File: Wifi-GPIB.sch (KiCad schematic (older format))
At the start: 10 parts

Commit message: Add ESP to sch
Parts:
- added U?: ESP-12/07v2/08v2, symbol ESP-12/07v2/08v2
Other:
- moved on the sheet: P?, U?
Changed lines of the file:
@@
 LIBS:open-project
 LIBS:mic5504
+LIBS:esp8266
+LIBS:Wifi-GPIB-cache
 EELAYER 25 0
 EELAYER END
@@
 L STM32F030C6 U?
 U 1 1 5564BC8B
-P 3950 4100
-F 0 "U?" H 2450 6000 60  0000 C CNN
-F 1 "STM32F030C6" H 5200 2200 60  0000 C CNN
-F 2 "LQFP48" H 3950 4100 40  0000 C CIN
-F 3 "" H 3950 4100 60  0000 C CNN
-	1    3950 4100
+P 2900 4550
+F 0 "U?" H 1400 6450 60  0000 C CNN
+F 1 "STM32F030C6" H 4150 2650 60  0000 C CNN
+F 2 "LQFP48" H 2900 4550 40  0000 C CIN
+F 3 "" H 2900 4550 60  0000 C CNN
+	1    2900 4550
 	1    0    0    -1
 $EndComp
@@
 L SN75160B U?
 U 1 1 5564BDA6
-P 7950 2350
-F 0 "U?" H 7950 2250 50  0000 C CNN
-F 1 "SN75160B" H 7950 2450 50  0000 C CNN
-F 2 "MODULE" H 7950 2350 50  0001 C CNN
-F 3 "DOCUMENTATION" H 7950 2350 50  0001 C CNN
-	1    7950 2350
+P 6950 3550
+F 0 "U?" H 6950 3450 50  0000 C CNN
+F 1 "SN75160B" H 6950 3650 50  0000 C CNN
+F 2 "MODULE" H 6950 3550 50  0001 C CNN
+F 3 "DOCUMENTATION" H 6950 3550 50  0001 C CNN
+	1    6950 3550
 	1    0    0    -1
 $EndComp
@@
 L SN75162B U?
 U 1 1 5564BE4F
-P 7950 4300
-F 0 "U?" H 7950 4200 50  0000 C CNN
-F 1 "SN75162B" H 7950 4400 50  0000 C CNN
-F 2 "MODULE" H 7950 4300 50  0001 C CNN
-F 3 "DOCUMENTATION" H 7950 4300 50  0001 C CNN
-	1    7950 4300
+P 6950 5500
+F 0 "U?" H 6950 5400 50  0000 C CNN
+F 1 "SN75162B" H 6950 5600 50  0000 C CNN
+F 2 "MODULE" H 6950 5500 50  0001 C CNN
+F 3 "DOCUMENTATION" H 6950 5500 50  0001 C CNN
+	1    6950 5500
 	1    0    0    -1
 $EndComp
@@
 L CONN_CENTRONICS_24 P?
 U 1 1 5564D4E2
-P 10350 3300
-F 0 "P?" H 10350 3950 60  0000 C CNN
-F 1 "CONN_CENTRONICS_24" V 10350 3300 50  0000 C CNN
-F 2 "" H 10350 3300 60  0000 C CNN
-F 3 "" H 10350 3300 60  0000 C CNN
-	1    10350 3300
+P 10300 3750
+F 0 "P?" H 10300 4400 60  0000 C CNN
+F 1 "CONN_CENTRONICS_24" V 10300 3750 50  0000 C CNN
+F 2 "" H 10300 3750 60  0000 C CNN
+F 3 "" H 10300 3750 60  0000 C CNN
+	1    10300 3750
 	1    0    0    -1
 $EndComp
@@
 	1    0    0    -1
 $EndComp
+$Comp
+L ESP-12/07v2/08v2 U?
+U 1 1 5564D82B
+P 5450 1600
+F 0 "U?" H 5450 2150 60  0000 C CNN
+F 1 "ESP-12/07v2/08v2" H 5450 1050 60  0000 C CNN
+F 2 "" H 5450 1600 60  0000 C CNN
+F 3 "" H 5450 1600 60  0000 C CNN
+	1    5450 1600
+	1    0    0    -1
+$EndComp

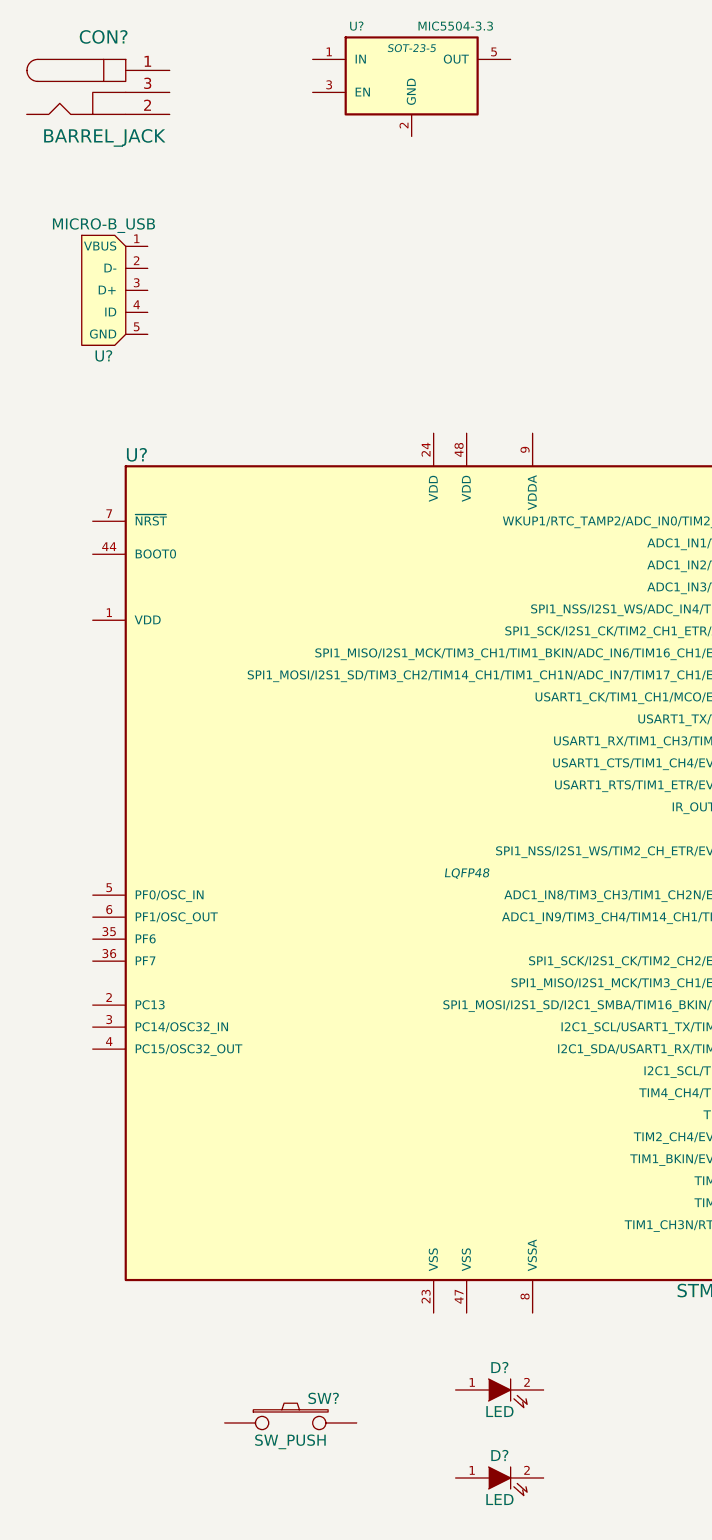
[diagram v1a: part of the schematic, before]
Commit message: Add new voltage regulator to sch
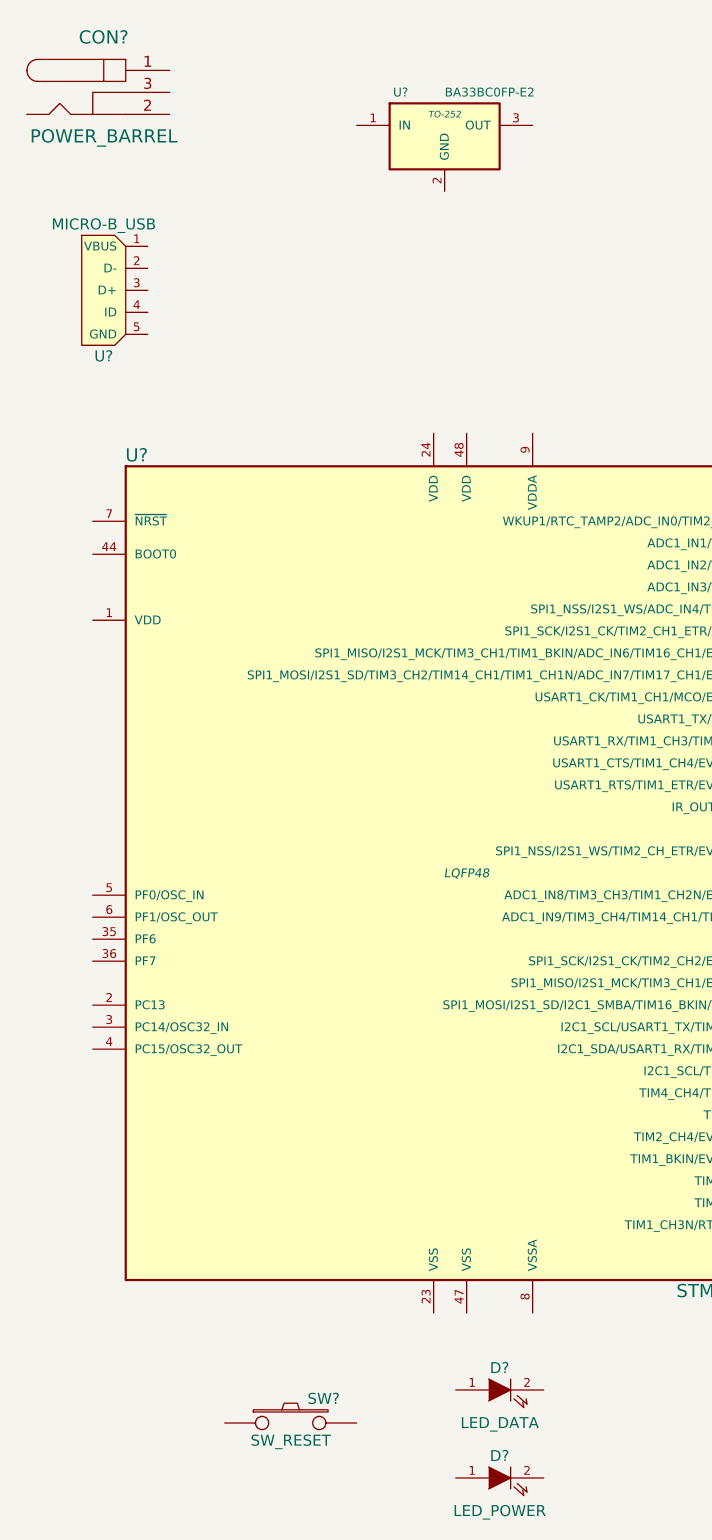
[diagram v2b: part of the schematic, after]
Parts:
- removed U?: MIC5504-3.3, SOT-23-5, symbol MIC5504-3.3
- added U?: BA33BC0FP-E2, TO-252, symbol BA33BC0FP-E2
- CON?: value BARREL_JACK -> POWER_BARREL
- D?: value LED -> LED_DATA
- D?: value LED -> LED_POWER
- SW?: value SW_PUSH -> SW_RESET
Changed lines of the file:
@@
 LIBS:conn_centronics_24
 LIBS:open-project
-LIBS:mic5504
 LIBS:esp8266
+LIBS:ba33bc0fp-e2
 LIBS:Wifi-GPIB-cache
 EELAYER 25 0
@@
 P 2100 7050
 F 0 "SW?" H 2250 7160 50  0000 C CNN
-F 1 "SW_PUSH" H 2100 6970 50  0000 C CNN
+F 1 "SW_RESET" H 2100 6970 50  0000 C CNN
 F 2 "" H 2100 7050 60  0000 C CNN
 F 3 "" H 2100 7050 60  0000 C CNN
@@
 P 3050 6900
 F 0 "D?" H 3050 7000 50  0000 C CNN
-F 1 "LED" H 3050 6800 50  0000 C CNN
+F 1 "LED_DATA" H 3050 6750 50  0000 C CNN
 F 2 "" H 3050 6900 60  0000 C CNN
 F 3 "" H 3050 6900 60  0000 C CNN
@@
 P 3050 7300
 F 0 "D?" H 3050 7400 50  0000 C CNN
-F 1 "LED" H 3050 7200 50  0000 C CNN
+F 1 "LED_POWER" H 3050 7150 50  0000 C CNN
 F 2 "" H 3050 7300 60  0000 C CNN
 F 3 "" H 3050 7300 60  0000 C CNN
@@
 P 1250 1000
 F 0 "CON?" H 1250 1250 60  0000 C CNN
-F 1 "BARREL_JACK" H 1250 800 60  0000 C CNN
+F 1 "POWER_BARREL" H 1250 800 60  0000 C CNN
 F 2 "" H 1250 1000 60  0000 C CNN
 F 3 "" H 1250 1000 60  0000 C CNN
@@
 $EndComp
 $Comp
-L MIC5504-3.3 U?
-U 1 1 5564E907
-P 2650 900
-F 0 "U?" H 2400 1100 40  0000 C CNN
-F 1 "MIC5504-3.3" H 2850 1100 40  0000 C CNN
-F 2 "SOT-23-5" H 2650 1000 35  0000 C CIN
-F 3 "" H 2650 900 60  0000 C CNN
-	1    2650 900
-	1    0    0    -1
-$EndComp
-$Comp
 L ESP-12/07v2/08v2 U?
 U 1 1 5564D82B
@@
 	1    0    0    -1
 $EndComp
+$Comp
+L BA33BC0FP-E2 U?
+U 1 1 5564E643
+P 2800 1200
+F 0 "U?" H 2600 1400 40  0000 C CNN
+F 1 "BA33BC0FP-E2" H 2800 1400 40  0000 L CNN
+F 2 "TO-252" H 2800 1300 30  0000 C CIN
+F 3 "" H 2800 1200 60  0000 C CNN
+	1    2800 1200
+	1    0    0    -1
+$EndComp

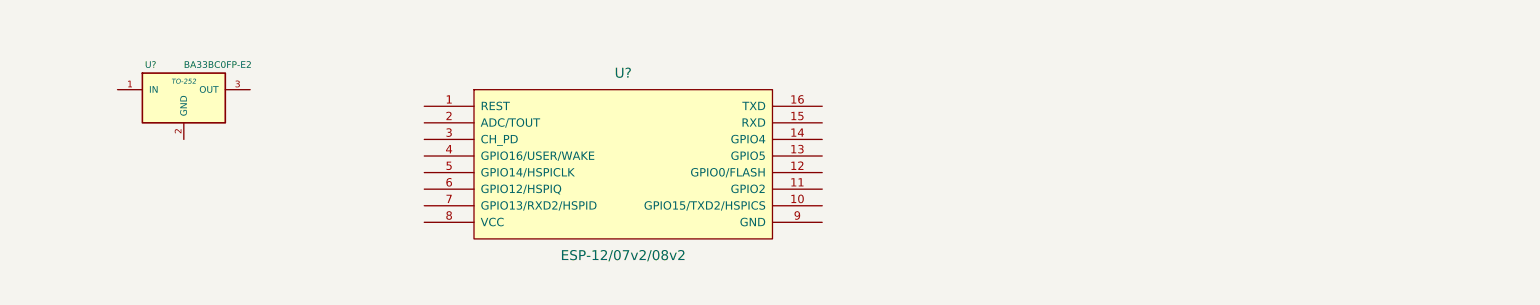
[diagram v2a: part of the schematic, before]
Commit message: Add power test points and add ESP programming header
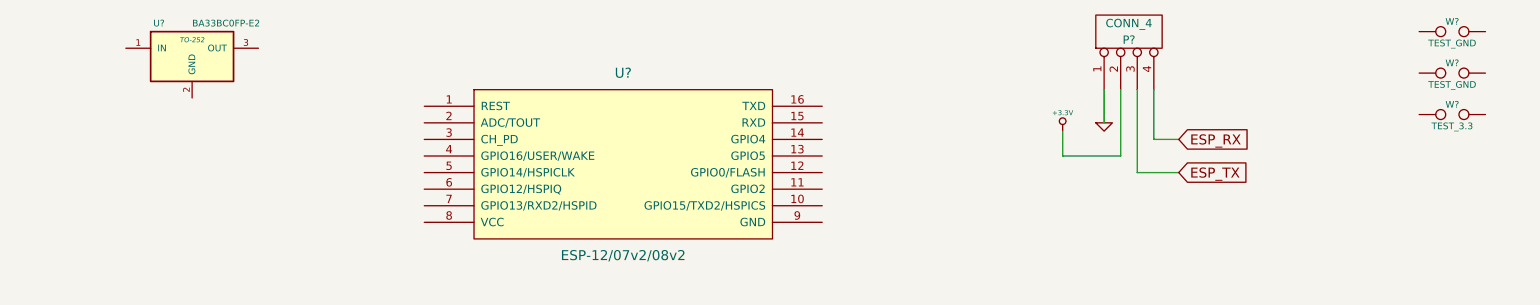
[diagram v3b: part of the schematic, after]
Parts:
- added P?: CONN_4, symbol CONN_4
- added W? (x2): TEST_GND, symbol TEST
- added W?: TEST_3.3, symbol TEST
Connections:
- new net +3.3V: P?.2 (P2)
- new net ESP_RX: P?.4 (P4)
- new net ESP_TX: P?.3 (P3)
- new net GND: P?.1 (P1)
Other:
- moved on the sheet: U?
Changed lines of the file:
@@
 L BA33BC0FP-E2 U?
 U 1 1 5564E643
-P 2800 1200
-F 0 "U?" H 2600 1400 40  0000 C CNN
-F 1 "BA33BC0FP-E2" H 2800 1400 40  0000 L CNN
-F 2 "TO-252" H 2800 1300 30  0000 C CIN
-F 3 "" H 2800 1200 60  0000 C CNN
-	1    2800 1200
+P 2850 950
+F 0 "U?" H 2650 1150 40  0000 C CNN
+F 1 "BA33BC0FP-E2" H 2850 1150 40  0000 L CNN
+F 2 "TO-252" H 2850 1050 30  0000 C CIN
+F 3 "" H 2850 950 60  0000 C CNN
+	1    2850 950
 	1    0    0    -1
 $EndComp
+$Comp
+L CONN_4 P?
+U 1 1 5564EAE9
+P 8500 800
+F 0 "P?" V 8450 800 50  0000 C CNN
+F 1 "CONN_4" V 8550 800 50  0000 C CNN
+F 2 "" H 8500 800 60  0000 C CNN
+F 3 "" H 8500 800 60  0000 C CNN
+	1    8500 800
+	0    -1   -1   0
+$EndComp
+$Comp
+L GND #PWR?
+U 1 1 5564ECD5
+P 8350 1350
+F 0 "#PWR?" H 8350 1350 30  0001 C CNN
+F 1 "GND" H 8350 1280 30  0001 C CNN
+F 2 "" H 8350 1350 60  0000 C CNN
+F 3 "" H 8350 1350 60  0000 C CNN
+	1    8350 1350
+	1    0    0    -1
+$EndComp
+Wire Wire Line
+	8350 1150 8350 1350
+$Comp
+L +3.3V #PWR?
+U 1 1 5564EE5E
+P 8100 1400
+F 0 "#PWR?" H 8100 1360 30  0001 C CNN
+F 1 "+3.3V" H 8100 1510 30  0000 C CNN
+F 2 "" H 8100 1400 60  0000 C CNN
+F 3 "" H 8100 1400 60  0000 C CNN
+	1    8100 1400
+	1    0    0    -1
+$EndComp
+Wire Wire Line
+	8100 1400 8100 1550
+Wire Wire Line
+	8100 1550 8450 1550
+Wire Wire Line
+	8450 1550 8450 1150
+Wire Wire Line
+	8550 1150 8550 1650
+Wire Wire Line
+	8650 1150 8650 1450
+Wire Wire Line
+	8650 1450 8800 1450
+Wire Wire Line
+	8550 1650 8800 1650
+Text GLabel 8800 1450 2    60   Input ~ 0
+ESP_RX
+Text GLabel 8800 1650 2    60   Input ~ 0
+ESP_TX
+$Comp
+L TEST W?
+U 1 1 5564EF1E
+P 10450 800
+F 0 "W?" H 10450 860 40  0000 C CNN
+F 1 "TEST_GND" H 10450 730 40  0000 C CNN
+F 2 "" H 10450 800 60  0000 C CNN
+F 3 "" H 10450 800 60  0000 C CNN
+	1    10450 800
+	1    0    0    -1
+$EndComp
+$Comp
+L TEST W?
+U 1 1 5564F521
+P 10450 1050
+F 0 "W?" H 10450 1110 40  0000 C CNN
+F 1 "TEST_GND" H 10450 980 40  0000 C CNN
+F 2 "" H 10450 1050 60  0000 C CNN
+F 3 "" H 10450 1050 60  0000 C CNN
+	1    10450 1050
+	1    0    0    -1
+$EndComp
+$Comp
+L TEST W?
+U 1 1 5564F6BC
+P 10450 1300
+F 0 "W?" H 10450 1360 40  0000 C CNN
+F 1 "TEST_3.3" H 10450 1230 40  0000 C CNN
+F 2 "" H 10450 1300 60  0000 C CNN
+F 3 "" H 10450 1300 60  0000 C CNN
+	1    10450 1300
+	1    0    0    -1
+$EndComp

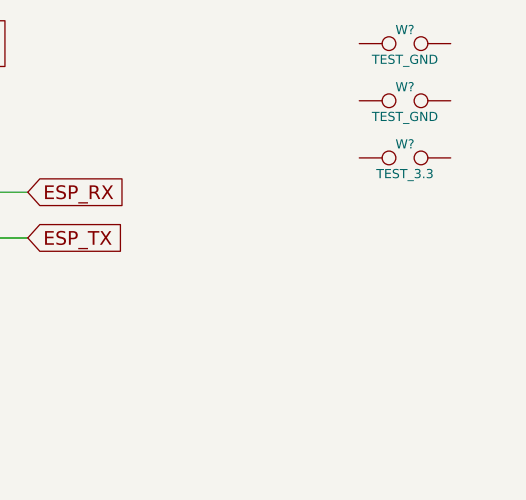
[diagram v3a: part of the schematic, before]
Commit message: Add Vin test point
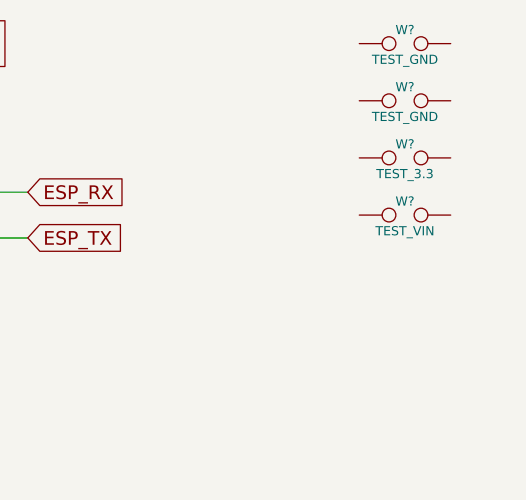
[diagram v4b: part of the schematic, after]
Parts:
- added W?: TEST_VIN, symbol TEST
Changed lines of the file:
@@
+	1    0    0    -1
+$EndComp
+$Comp
+L TEST W?
+U 1 1 5564F9AB
+P 10450 1550
+F 0 "W?" H 10450 1610 40  0000 C CNN
+F 1 "TEST_VIN" H 10450 1480 40  0000 C CNN
+F 2 "" H 10450 1550 60  0000 C CNN
+F 3 "" H 10450 1550 60  0000 C CNN
+	1    10450 1550
 	1    0    0    -1
 $EndComp

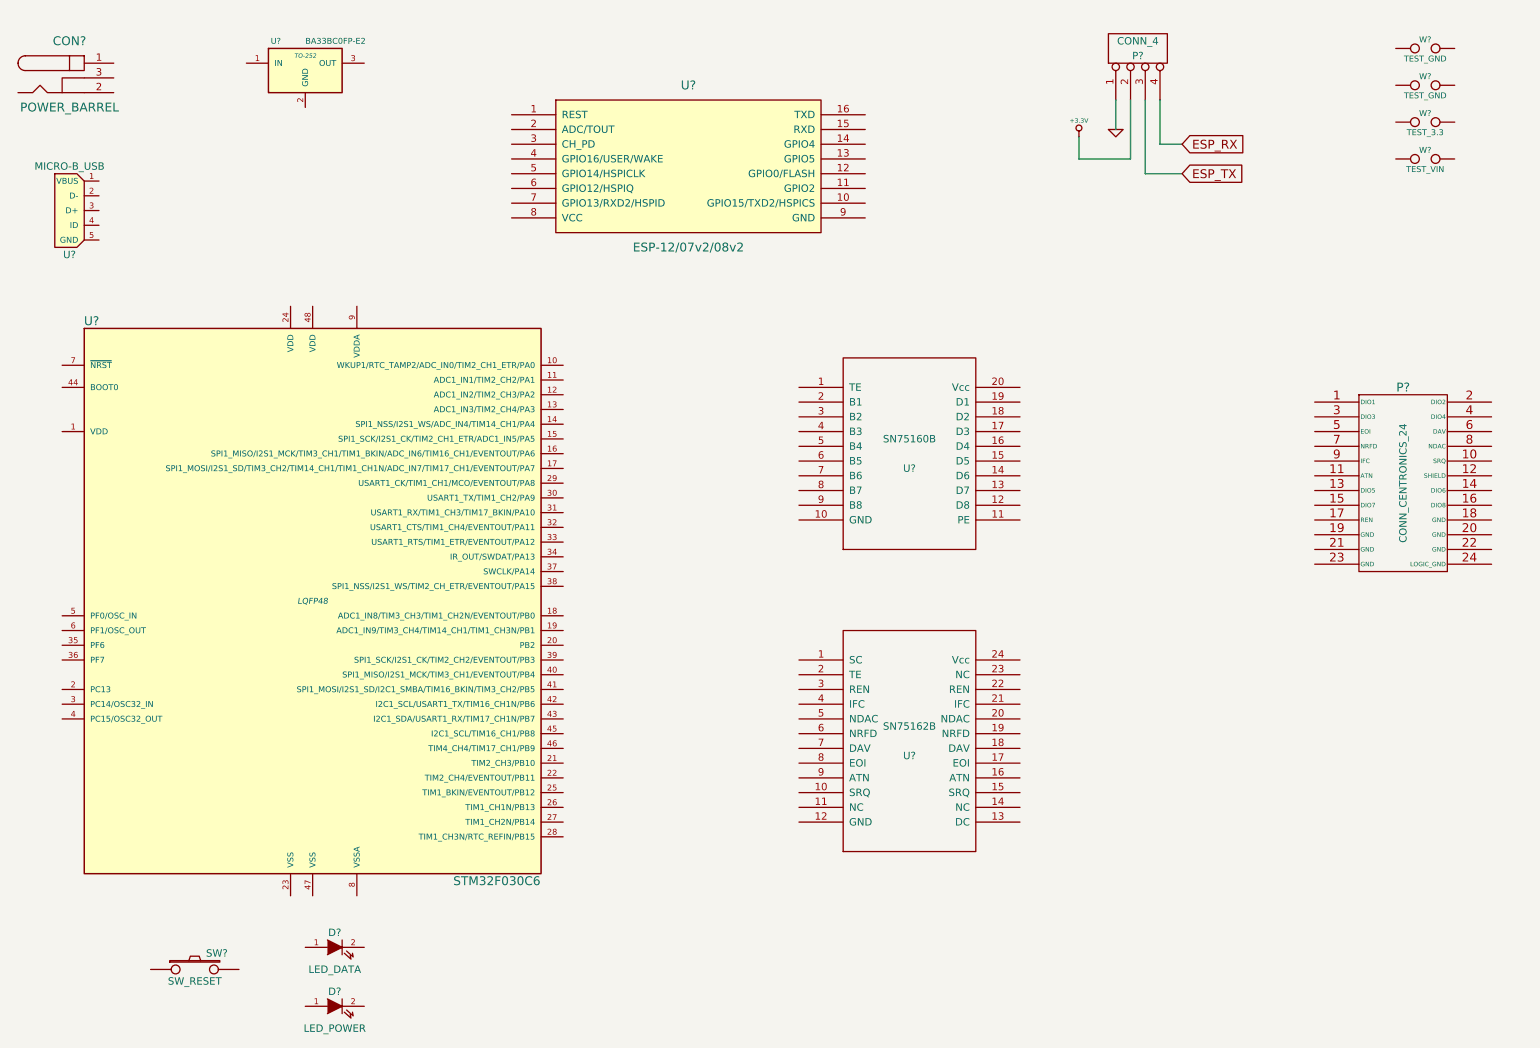
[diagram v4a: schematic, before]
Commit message: ESP mostly wired up. Need to decide on M0 -> ESP interface
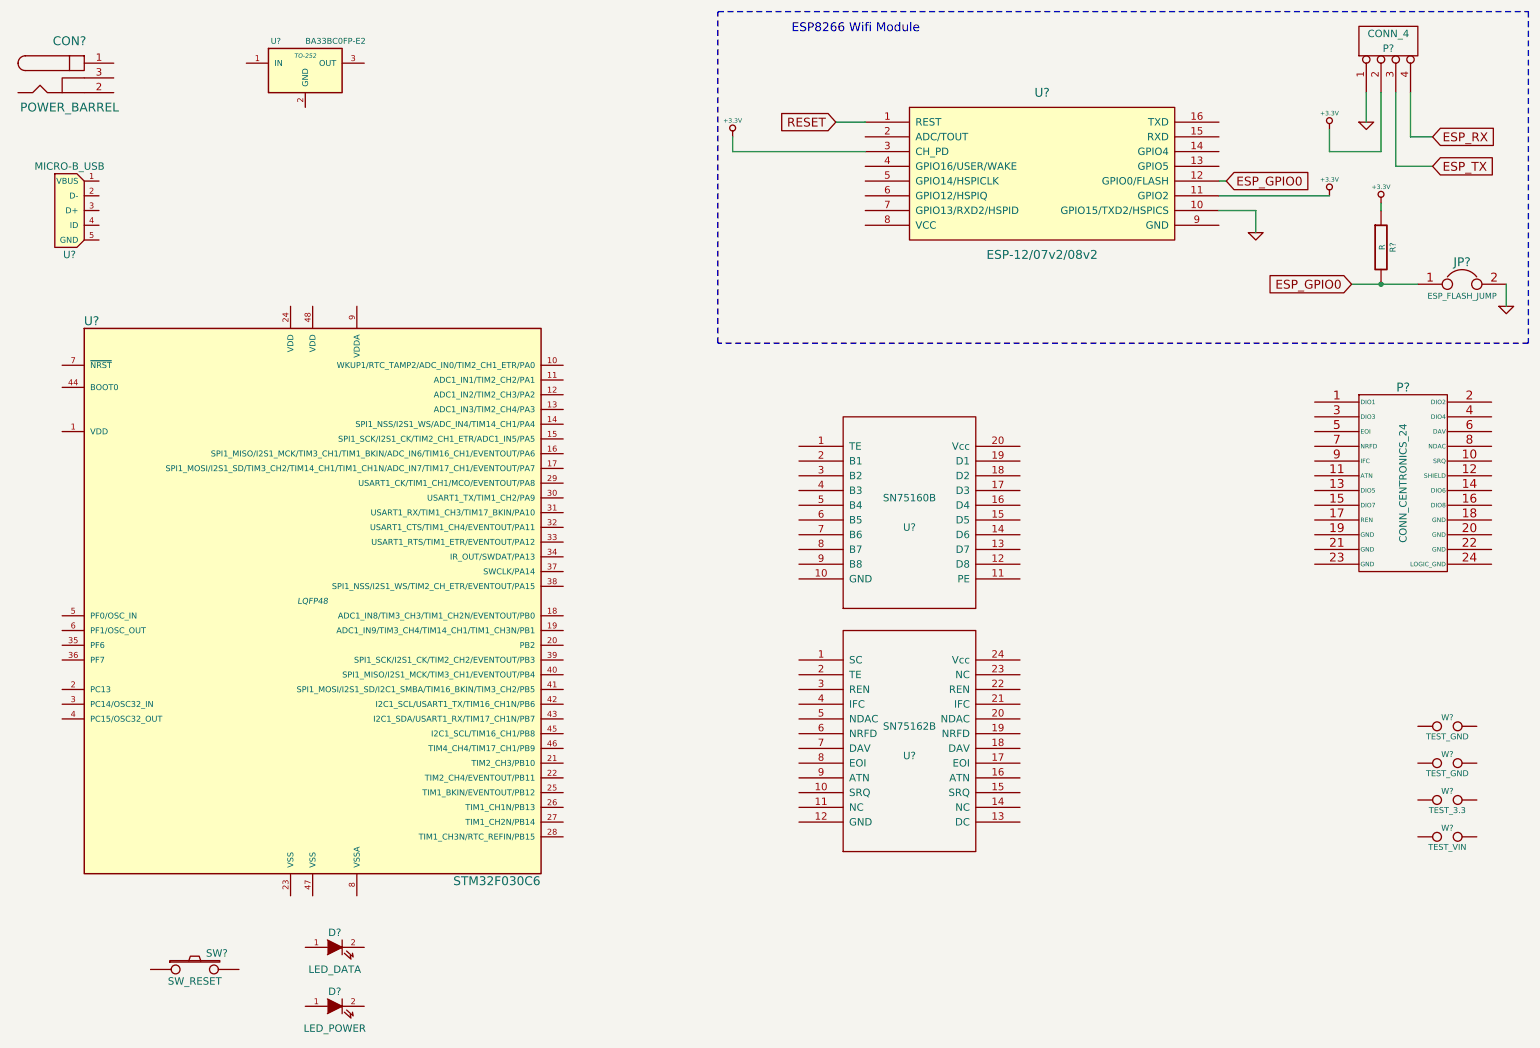
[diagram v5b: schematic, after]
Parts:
- added JP?: ESP_FLASH_JUMP, symbol JUMPER
- added R?: R, symbol R
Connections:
- net +3.3V: now also U?.11 (GPIO2), U?.3 (CH_PD), R?.1
- net GND: now also U?.10 (GPIO15/TXD2/HSPICS), JP?.2
- net RESET: now reaches U?.1 (REST)
- net ESP_GPIO0: now reaches U?.12 (GPIO0/FLASH)
- net ESP_GPIO0: now also JP?.1, R?.2
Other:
- note added: "ESP8266 Wifi Module"
- moved on the sheet: P?, U?, W?
